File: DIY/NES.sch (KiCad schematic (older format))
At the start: 6 parts, among them J1 Conn_01x07, J2 Conn_01x07, J3 DB15_Female, J4 DB25_Male, U1 74AHCT125N, U2 74AHCT125N

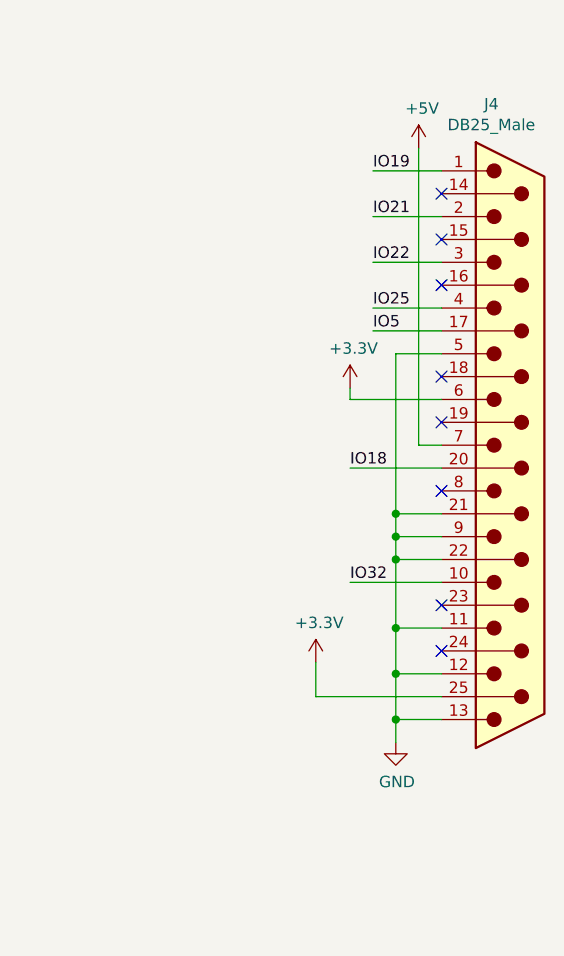
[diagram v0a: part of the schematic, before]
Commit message: [DIY] Update DIY & cable adapter schematic base on new DB25 mapping
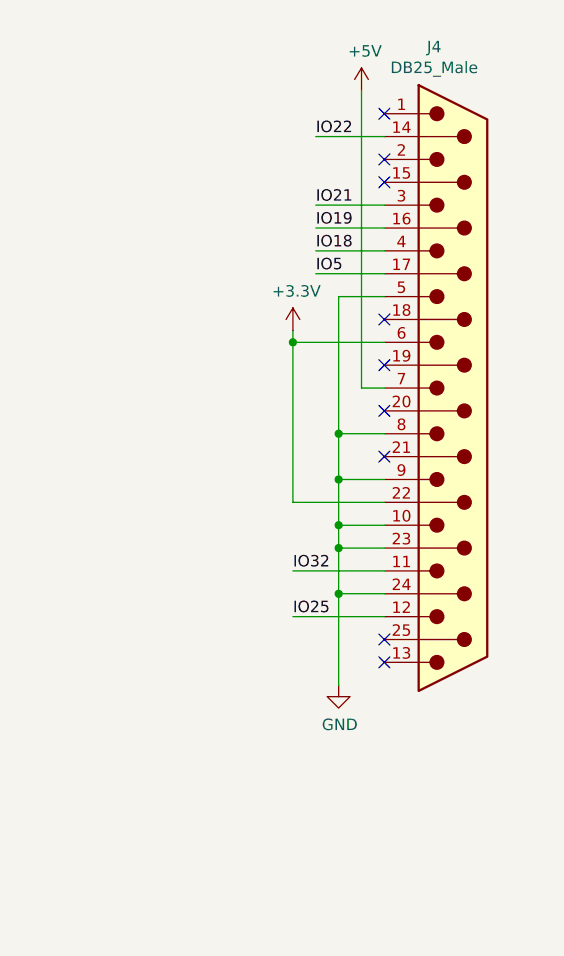
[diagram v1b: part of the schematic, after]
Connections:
- net +3V3: now also J4.22 (P22); no longer J4.25 (P25)
- net GND: now also J4.10, J4.23 (P23), J4.24 (P24), J4.8; no longer J4.11, J4.12, J4.13, J4.21 (P21), J4.22 (P22)
- net IO18: now also J4.4; no longer J4.20 (P20)
- net IO19: now also J4.16 (P16); no longer J4.1
- net IO21: now also J4.3; no longer J4.2
- net IO22: now also J4.14 (P14); no longer J4.3
- net IO25: now also J4.12; no longer J4.4
- net IO32: now also J4.11; no longer J4.10
- no-connect marks 27 -> 28
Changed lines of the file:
@@
 $Descr USLetter 11000 8500
 encoding utf-8
-Sheet 3 4
+Sheet 3 7
 Title "BlueRetro - Famicom/NES adapter cable"
-Date "2020-07-25"
-Rev "v1.0"
+Date "2020-08-22"
+Rev "v1.1"
 Comp ""
 Comment1 ""
@@
 $EndComp
 $Comp
-L Connector:DB25_Male J?
-U 1 1 5F23BC98
-P 10000 2850
-AR Path="/5F127084/5F23BC98" Ref="J?"  Part="1"
-AR Path="/5F1E85DD/5F23BC98" Ref="J4"  Part="1"
-F 0 "J4" H 9918 1358 50  0000 C CNN
-F 1 "DB25_Male" H 9918 1449 50  0000 C CNN
-F 2 "" H 10000 2850 50  0001 C CNN
-F 3 " ~" H 10000 2850 50  0001 C CNN
-	1    10000 2850
-	1    0    0    1
-$EndComp
-$Comp
 L 74xx:74LS125 U?
 U 1 1 5F23BCA4
@@
 F 3 "http://www.ti.com/general/docs/suppproductinfo.tsp?distId=10&gotoUrl=http%3A%2F%2Fwww.ti.com%2Flit%2Fgpn%2Fsn74ahct125" H 4150 5500 50  0001 C CNN
 	5    4150 5500
-	1    0    0    -1
-$EndComp
-Wire Wire Line
-	9400 1650 9700 1650
-Wire Wire Line
-	9400 1850 9700 1850
-Wire Wire Line
-	9400 2050 9700 2050
-Wire Wire Line
-	9400 2250 9700 2250
-$Comp
-L power:+5V #PWR?
-U 1 1 5F23BD02
-P 9600 1550
-AR Path="/5F127084/5F23BD02" Ref="#PWR?"  Part="1"
-AR Path="/5F1E85DD/5F23BD02" Ref="#PWR?"  Part="1"
-F 0 "#PWR?" H 9600 1400 50  0001 C CNN
-F 1 "+5V" H 9615 1723 50  0000 C CNN
-F 2 "" H 9600 1550 50  0001 C CNN
-F 3 "" H 9600 1550 50  0001 C CNN
-	1    9600 1550
-	1    0    0    -1
-$EndComp
-$Comp
-L power:GND #PWR?
-U 1 1 5F23BD08
-P 9500 4150
-AR Path="/5F127084/5F23BD08" Ref="#PWR?"  Part="1"
-AR Path="/5F1E85DD/5F23BD08" Ref="#PWR?"  Part="1"
-F 0 "#PWR?" H 9500 3900 50  0001 C CNN
-F 1 "GND" H 9505 3977 50  0000 C CNN
-F 2 "" H 9500 4150 50  0001 C CNN
-F 3 "" H 9500 4150 50  0001 C CNN
-	1    9500 4150
-	1    0    0    -1
-$EndComp
-Wire Wire Line
-	9700 2450 9500 2450
-Wire Wire Line
-	9500 2450 9500 3150
-Wire Wire Line
-	9700 3250 9500 3250
-Connection ~ 9500 3250
-Wire Wire Line
-	9600 1550 9600 2850
-Wire Wire Line
-	9600 2850 9700 2850
-$Comp
-L power:+3.3V #PWR?
-U 1 1 5F23BD18
-P 9300 2600
-AR Path="/5F127084/5F23BD18" Ref="#PWR?"  Part="1"
-AR Path="/5F1E85DD/5F23BD18" Ref="#PWR?"  Part="1"
-F 0 "#PWR?" H 9300 2450 50  0001 C CNN
-F 1 "+3.3V" H 9315 2773 50  0000 C CNN
-F 2 "" H 9300 2600 50  0001 C CNN
-F 3 "" H 9300 2600 50  0001 C CNN
-	1    9300 2600
 	1    0    0    -1
 $EndComp
@@
 	1    0    0    -1
 $EndComp
-Text Label 9400 1650 0    50   ~ 0
-IO19
-Text Label 9400 1850 0    50   ~ 0
-IO21
-Text Label 9400 2050 0    50   ~ 0
-IO22
-Text Label 9400 2250 0    50   ~ 0
-IO25
-Wire Wire Line
-	9700 2350 9400 2350
-Wire Wire Line
-	9300 2650 9300 2600
-Wire Wire Line
-	9300 2650 9700 2650
-Wire Wire Line
-	9300 2950 9700 2950
-NoConn ~ 9700 1950
-NoConn ~ 9700 2550
-NoConn ~ 9700 2750
-NoConn ~ 9700 3050
-Text Label 9400 2350 0    50   ~ 0
-IO5
-Text Label 9300 2950 0    50   ~ 0
-IO18
 $Comp
 L Connector:DB15_Female J3
@@
 NoConn ~ 1500 2250
 NoConn ~ 1500 2350
-Wire Wire Line
-	9500 3250 9500 3350
-$Comp
-L power:+3.3V #PWR?
-U 1 1 5F23310B
-P 9150 3800
-AR Path="/5F127084/5F23310B" Ref="#PWR?"  Part="1"
-AR Path="/5F1E85DD/5F23310B" Ref="#PWR?"  Part="1"
-F 0 "#PWR?" H 9150 3650 50  0001 C CNN
-F 1 "+3.3V" H 9165 3973 50  0000 C CNN
-F 2 "" H 9150 3800 50  0001 C CNN
-F 3 "" H 9150 3800 50  0001 C CNN
-	1    9150 3800
-	1    0    0    -1
-$EndComp
-Wire Wire Line
-	9700 3950 9150 3950
-Wire Wire Line
-	9150 3950 9150 3800
-Wire Wire Line
-	9700 4050 9500 4050
-Connection ~ 9500 4050
-Wire Wire Line
-	9500 4050 9500 4150
-Wire Wire Line
-	9700 3850 9500 3850
-Connection ~ 9500 3850
-Wire Wire Line
-	9500 3850 9500 4050
-Wire Wire Line
-	9700 3650 9500 3650
-Connection ~ 9500 3650
-Wire Wire Line
-	9500 3650 9500 3850
-Wire Wire Line
-	9700 3450 9300 3450
-Text Label 9300 3450 0    50   ~ 0
-IO32
-NoConn ~ 9700 1750
-NoConn ~ 9700 2150
-Wire Wire Line
-	9700 3150 9500 3150
-Connection ~ 9500 3150
-Wire Wire Line
-	9500 3150 9500 3250
-Wire Wire Line
-	9700 3350 9500 3350
-Connection ~ 9500 3350
-Wire Wire Line
-	9500 3350 9500 3650
-NoConn ~ 9700 3550
-NoConn ~ 9700 3750
 Text Label 3550 1350 0    50   ~ 0
 IO19
@@
 $EndComp
 NoConn ~ 7200 4100
+$Comp
+L Connector:DB25_Male J?
+U 1 1 5F70CF6E
+P 9750 2600
+AR Path="/5F127084/5F70CF6E" Ref="J?"  Part="1"
+AR Path="/5F1E85DD/5F70CF6E" Ref="J4"  Part="1"
+AR Path="/5F2C5C0D/5F70CF6E" Ref="J?"  Part="1"
+F 0 "J4" H 9668 1108 50  0000 C CNN
+F 1 "DB25_Male" H 9668 1199 50  0000 C CNN
+F 2 "" H 9750 2600 50  0001 C CNN
+F 3 " ~" H 9750 2600 50  0001 C CNN
+	1    9750 2600
+	1    0    0    1
+$EndComp
+Wire Wire Line
+	9150 1800 9450 1800
+Wire Wire Line
+	9150 2000 9450 2000
+$Comp
+L power:+5V #PWR?
+U 1 1 5F70CF77
+P 9350 1300
+AR Path="/5F127084/5F70CF77" Ref="#PWR?"  Part="1"
+AR Path="/5F1E85DD/5F70CF77" Ref="#PWR?"  Part="1"
+AR Path="/5F2C5C0D/5F70CF77" Ref="#PWR?"  Part="1"
+F 0 "#PWR?" H 9350 1150 50  0001 C CNN
+F 1 "+5V" H 9365 1473 50  0000 C CNN
+F 2 "" H 9350 1300 50  0001 C CNN
+F 3 "" H 9350 1300 50  0001 C CNN
+	1    9350 1300
+	1    0    0    -1
+$EndComp
+$Comp
+L power:GND #PWR?
+U 1 1 5F70CF7D
+P 9250 3900
+AR Path="/5F127084/5F70CF7D" Ref="#PWR?"  Part="1"
+AR Path="/5F1E85DD/5F70CF7D" Ref="#PWR?"  Part="1"
+AR Path="/5F2C5C0D/5F70CF7D" Ref="#PWR?"  Part="1"
+F 0 "#PWR?" H 9250 3650 50  0001 C CNN
+F 1 "GND" H 9255 3727 50  0000 C CNN
+F 2 "" H 9250 3900 50  0001 C CNN
+F 3 "" H 9250 3900 50  0001 C CNN
+	1    9250 3900
+	1    0    0    -1
+$EndComp
+Wire Wire Line
+	9450 2200 9250 2200
+Wire Wire Line
+	9450 3000 9250 3000
+Wire Wire Line
+	9350 1300 9350 2600
+Wire Wire Line
+	9350 2600 9450 2600
+$Comp
+L power:+3.3V #PWR?
+U 1 1 5F70CF87
+P 9050 2350
+AR Path="/5F127084/5F70CF87" Ref="#PWR?"  Part="1"
+AR Path="/5F1E85DD/5F70CF87" Ref="#PWR?"  Part="1"
+AR Path="/5F2C5C0D/5F70CF87" Ref="#PWR?"  Part="1"
+F 0 "#PWR?" H 9050 2200 50  0001 C CNN
+F 1 "+3.3V" H 9065 2523 50  0000 C CNN
+F 2 "" H 9050 2350 50  0001 C CNN
+F 3 "" H 9050 2350 50  0001 C CNN
+	1    9050 2350
+	1    0    0    -1
+$EndComp
+Text Label 9150 1900 0    50   ~ 0
+IO19
+Text Label 9150 1800 0    50   ~ 0
+IO21
+Text Label 9150 1500 0    50   ~ 0
+IO22
+Text Label 9050 3600 0    50   ~ 0
+IO25
+Wire Wire Line
+	9450 2100 9150 2100
+Wire Wire Line
+	9050 2400 9050 2350
+Wire Wire Line
+	9050 2400 9450 2400
+Text Label 9150 2100 0    50   ~ 0
+IO5
+Text Label 9150 2000 0    50   ~ 0
+IO18
+Text Label 9050 3400 0    50   ~ 0
+IO32
+Wire Wire Line
+	9250 2200 9250 2800
+Wire Wire Line
+	9250 3900 9250 3500
+Connection ~ 9250 3000
+Wire Wire Line
+	9450 2800 9250 2800
+Connection ~ 9250 2800
+Wire Wire Line
+	9250 2800 9250 3000
+Wire Wire Line
+	9450 1900 9150 1900
+Wire Wire Line
+	9450 1500 9150 1500
+Wire Wire Line
+	9450 3600 9050 3600
+Wire Wire Line
+	9450 3400 9050 3400
+NoConn ~ 9450 3800
+NoConn ~ 9450 1600
+NoConn ~ 9450 1700
+NoConn ~ 9450 2300
+NoConn ~ 9450 2500
+NoConn ~ 9450 2700
+NoConn ~ 9450 2900
+Wire Wire Line
+	9450 3200 9250 3200
+Connection ~ 9250 3200
+Wire Wire Line
+	9450 3300 9250 3300
+Connection ~ 9250 3300
+Wire Wire Line
+	9250 3300 9250 3200
+Wire Wire Line
+	9450 3500 9250 3500
+Connection ~ 9250 3500
+Wire Wire Line
+	9250 3500 9250 3300
+NoConn ~ 9450 1400
+NoConn ~ 9450 3700
+Wire Wire Line
+	9250 3000 9250 3200
+Wire Wire Line
+	9450 3100 9050 3100
+Wire Wire Line
+	9050 3100 9050 2400
+Connection ~ 9050 2400
 $EndSCHEMATC

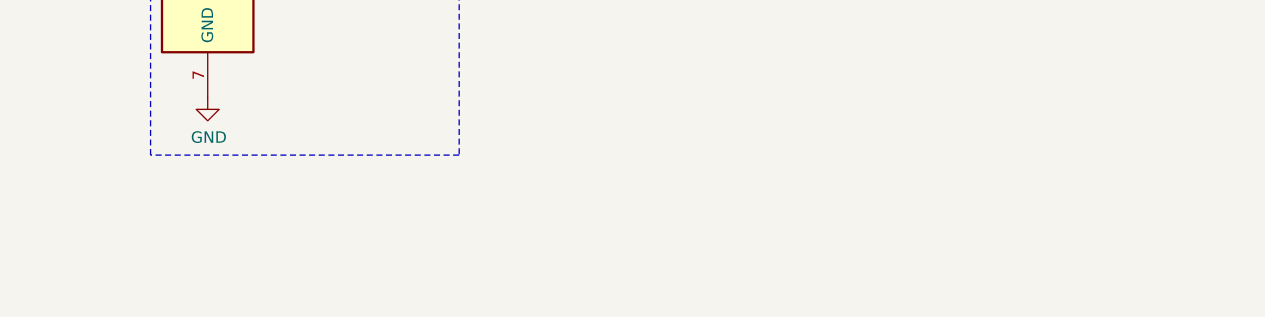
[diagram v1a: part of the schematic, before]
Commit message: [DIY] Add note to cable schematics to underline how important I39 is.
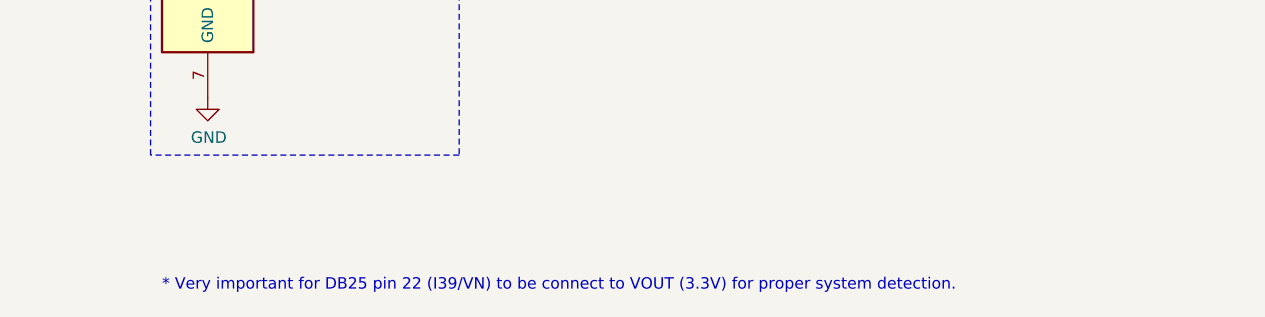
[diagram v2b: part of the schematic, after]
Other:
- note added: "* Very important for DB25 pin 22 (I39/VN) to be connect to VOUT (3.3V) for proper system detection."
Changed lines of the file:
@@
 	9050 3100 9050 2400
 Connection ~ 9050 2400
+Text Notes 6350 6900 0    50   ~ 0
+* Very important for DB25 pin 22 (I39/VN) to be connect to VOUT (3.3V) for proper system detection.
 $EndSCHEMATC

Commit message: Use new port symbol in cable schematic
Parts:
- J1, J2: symbol Connector_Generic:Conn_01x07 -> Connector_Gaming:NES
- J3: symbol Connector:DB15_Female -> Connector_Gaming:Atari5200_Famicom_NeoGeoAES_PCGamePort_DA15
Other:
- note added: "Connectors facing console"
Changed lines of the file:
@@
 Sheet 3 7
 Title "BlueRetro - Famicom/NES adapter cable"
-Date "2020-08-22"
-Rev "v1.1"
-Comp ""
+Date "2020-10-02"
+Rev "v1.2"
+Comp "©2020 Jacques Gagnon, licensed under CC-BY-4.0"
 Comment1 ""
 Comment2 ""
@@
 IO18
 $Comp
-L Connector_Generic:Conn_01x07 J?
-U 1 1 5F23BDF9
-P 1300 2050
-AR Path="/5F127084/5F23BDF9" Ref="J?"  Part="1"
-AR Path="/5F1E85DD/5F23BDF9" Ref="J1"  Part="1"
-F 0 "J1" H 1300 2600 50  0000 C CNN
-F 1 "Conn_01x07" H 1300 2500 50  0000 C CNN
-F 2 "" H 1300 2050 50  0001 C CNN
-F 3 "~" H 1300 2050 50  0001 C CNN
-	1    1300 2050
-	-1   0    0    -1
-$EndComp
-$Comp
-L Connector_Generic:Conn_01x07 J?
+L Connector_Gaming:NES J?
 U 1 1 5F23BDFF
-P 1300 3900
+P 1900 2900
 AR Path="/5F127084/5F23BDFF" Ref="J?"  Part="1"
 AR Path="/5F1E85DD/5F23BDFF" Ref="J2"  Part="1"
-F 0 "J2" H 1300 4450 50  0000 C CNN
-F 1 "Conn_01x07" H 1300 4350 50  0000 C CNN
-F 2 "" H 1300 3900 50  0001 C CNN
-F 3 "~" H 1300 3900 50  0001 C CNN
-	1    1300 3900
-	-1   0    0    -1
+F 0 "J2" H 1950 3250 50  0000 C CNN
+F 1 "Conn_01x07" H 1900 3350 50  0001 C CNN
+F 2 "" H 1900 2900 50  0001 C CNN
+F 3 "~" H 1900 2900 50  0001 C CNN
+	1    1900 2900
+	1    0    0    -1
 $EndComp
 $Comp
 L power:GND #PWR?
 U 1 1 5F23BE05
-P 1600 2450
+P 1600 2050
 AR Path="/5F127084/5F23BE05" Ref="#PWR?"  Part="1"
 AR Path="/5F1E85DD/5F23BE05" Ref="#PWR?"  Part="1"
-F 0 "#PWR?" H 1600 2200 50  0001 C CNN
-F 1 "GND" H 1605 2277 50  0000 C CNN
-F 2 "" H 1600 2450 50  0001 C CNN
-F 3 "" H 1600 2450 50  0001 C CNN
-	1    1600 2450
-	1    0    0    -1
+F 0 "#PWR?" H 1600 1800 50  0001 C CNN
+F 1 "GND" H 1605 1877 50  0000 C CNN
+F 2 "" H 1600 2050 50  0001 C CNN
+F 3 "" H 1600 2050 50  0001 C CNN
+	1    1600 2050
+	-1   0    0    -1
 $EndComp
 $Comp
 L power:GND #PWR?
 U 1 1 5F23BE0B
-P 1600 4300
+P 1600 3050
 AR Path="/5F127084/5F23BE0B" Ref="#PWR?"  Part="1"
 AR Path="/5F1E85DD/5F23BE0B" Ref="#PWR?"  Part="1"
-F 0 "#PWR?" H 1600 4050 50  0001 C CNN
-F 1 "GND" H 1605 4127 50  0000 C CNN
-F 2 "" H 1600 4300 50  0001 C CNN
-F 3 "" H 1600 4300 50  0001 C CNN
-	1    1600 4300
-	1    0    0    -1
+F 0 "#PWR?" H 1600 2800 50  0001 C CNN
+F 1 "GND" H 1605 2877 50  0000 C CNN
+F 2 "" H 1600 3050 50  0001 C CNN
+F 3 "" H 1600 3050 50  0001 C CNN
+	1    1600 3050
+	-1   0    0    -1
 $EndComp
 $Comp
 L power:+5V #PWR?
 U 1 1 5F23BE11
-P 1650 3450
+P 2300 2650
 AR Path="/5F127084/5F23BE11" Ref="#PWR?"  Part="1"
 AR Path="/5F1E85DD/5F23BE11" Ref="#PWR?"  Part="1"
-F 0 "#PWR?" H 1650 3300 50  0001 C CNN
-F 1 "+5V" H 1665 3623 50  0000 C CNN
-F 2 "" H 1650 3450 50  0001 C CNN
-F 3 "" H 1650 3450 50  0001 C CNN
-	1    1650 3450
+F 0 "#PWR?" H 2300 2500 50  0001 C CNN
+F 1 "+5V" H 2315 2823 50  0000 C CNN
+F 2 "" H 2300 2650 50  0001 C CNN
+F 3 "" H 2300 2650 50  0001 C CNN
+	1    2300 2650
 	1    0    0    -1
 $EndComp
@@
 L power:+5V #PWR?
 U 1 1 5F23BE17
-P 1650 1600
+P 2300 1700
 AR Path="/5F127084/5F23BE17" Ref="#PWR?"  Part="1"
 AR Path="/5F1E85DD/5F23BE17" Ref="#PWR?"  Part="1"
-F 0 "#PWR?" H 1650 1450 50  0001 C CNN
-F 1 "+5V" H 1665 1773 50  0000 C CNN
-F 2 "" H 1650 1600 50  0001 C CNN
-F 3 "" H 1650 1600 50  0001 C CNN
-	1    1650 1600
-	1    0    0    -1
-$EndComp
-$Comp
-L Connector:DB15_Female J3
+F 0 "#PWR?" H 2300 1550 50  0001 C CNN
+F 1 "+5V" H 2315 1873 50  0000 C CNN
+F 2 "" H 2300 1700 50  0001 C CNN
+F 3 "" H 2300 1700 50  0001 C CNN
+	1    2300 1700
+	1    0    0    -1
+$EndComp
+$Comp
+L Connector_Gaming:Atari5200_Famicom_NeoGeoAES_PCGamePort_DA15 J3
 U 1 1 5F2B655C
-P 1200 6100
-F 0 "J3" H 1106 7092 50  0000 C CNN
-F 1 "DB15_Female" H 1106 7001 50  0000 C CNN
-F 2 "" H 1200 6100 50  0001 C CNN
-F 3 " ~" H 1200 6100 50  0001 C CNN
-	1    1200 6100
-	-1   0    0    -1
-$EndComp
-Wire Wire Line
-	1500 6300 1800 6300
-Wire Wire Line
-	1500 6600 1800 6600
-Text Notes 750  5050 0    50   ~ 0
+P 1900 4250
+F 0 "J3" H 1900 3400 50  0000 C CNN
+F 1 "DB15_Female" H 1806 5151 50  0001 C CNN
+F 2 "" H 1900 4250 50  0001 C CNN
+F 3 " ~" H 1900 4250 50  0001 C CNN
+	1    1900 4250
+	-1   0    0    1
+$EndComp
+Wire Wire Line
+	2200 4450 2500 4450
+Wire Wire Line
+	2200 4750 2500 4750
+Text Notes 1450 3200 0    50   ~ 0
 *Optional (only for Famicom 4P)
-NoConn ~ 1500 5400
-NoConn ~ 1500 5500
-NoConn ~ 1500 5600
-NoConn ~ 1500 5700
-NoConn ~ 1500 5800
-NoConn ~ 1500 5900
-NoConn ~ 1500 6000
-NoConn ~ 1500 6100
-NoConn ~ 1500 6200
-NoConn ~ 1500 6400
-NoConn ~ 1500 6500
-NoConn ~ 1500 6700
-NoConn ~ 1500 6800
-Text Label 1800 6300 2    50   ~ 0
+NoConn ~ 2200 3550
+NoConn ~ 2200 3650
+NoConn ~ 2200 3750
+NoConn ~ 2200 3850
+NoConn ~ 2200 3950
+NoConn ~ 2200 4050
+NoConn ~ 2200 4150
+NoConn ~ 2200 4250
+NoConn ~ 2200 4350
+NoConn ~ 2200 4550
+NoConn ~ 2200 4650
+NoConn ~ 2200 4850
+NoConn ~ 2200 4950
+Text Label 2500 4450 2    50   ~ 0
 P1-D1
-Text Label 1800 6600 2    50   ~ 0
+Text Label 2500 4750 2    50   ~ 0
 P2-D1
 Wire Wire Line
-	1500 3600 1600 3600
-Wire Wire Line
-	1500 4000 1650 4000
-Wire Wire Line
-	1650 4000 1650 3450
-Text Label 2000 3700 2    50   ~ 0
+	1700 2700 1600 2700
+Text Label 1200 2800 0    50   ~ 0
 P2-CUP
 Wire Wire Line
-	1500 3700 2000 3700
-Wire Wire Line
-	1500 3900 2000 3900
-NoConn ~ 1500 4100
-NoConn ~ 1500 4200
-NoConn ~ 1500 3800
-Text Label 2000 3900 2    50   ~ 0
+	1700 2800 1200 2800
+Wire Wire Line
+	1700 3000 1200 3000
+NoConn ~ 2200 2900
+NoConn ~ 2200 3000
+NoConn ~ 1700 2900
+Text Label 1200 3000 0    50   ~ 0
 P2-D0
 Wire Wire Line
-	1600 3600 1600 4300
-Wire Wire Line
-	1500 2150 1650 2150
-Wire Wire Line
-	1650 1600 1650 2150
-Wire Wire Line
-	1500 1750 1600 1750
-Wire Wire Line
-	1600 1750 1600 2450
-Wire Wire Line
-	1500 1850 2000 1850
-Wire Wire Line
-	1500 1950 2000 1950
-Wire Wire Line
-	1500 2050 2000 2050
-Text Label 2000 1850 2    50   ~ 0
+	1600 2700 1600 3050
+Wire Wire Line
+	1700 1700 1600 1700
+Wire Wire Line
+	1700 1800 1200 1800
+Text Label 1200 1800 0    50   ~ 0
 P1-CUP
-Text Label 2000 1950 2    50   ~ 0
+Text Label 1200 1900 0    50   ~ 0
 OUT0
-Text Label 2000 2050 2    50   ~ 0
+Text Label 1200 2000 0    50   ~ 0
 P1-D0
-NoConn ~ 1500 2250
-NoConn ~ 1500 2350
+NoConn ~ 2200 1900
+NoConn ~ 2200 2000
 Text Label 3550 1350 0    50   ~ 0
 IO19
@@
 Text Notes 6350 6900 0    50   ~ 0
 * Very important for DB25 pin 22 (I39/VN) to be connect to VOUT (3.3V) for proper system detection.
+Wire Wire Line
+	1700 2000 1200 2000
+Wire Wire Line
+	1700 1900 1200 1900
+Wire Wire Line
+	1600 1700 1600 2050
+$Comp
+L Connector_Gaming:NES J?
+U 1 1 5F23BDF9
+P 1900 1900
+AR Path="/5F127084/5F23BDF9" Ref="J?"  Part="1"
+AR Path="/5F1E85DD/5F23BDF9" Ref="J1"  Part="1"
+F 0 "J1" H 1950 2250 50  0000 C CNN
+F 1 "Conn_01x07" H 1900 2350 50  0001 C CNN
+F 2 "" H 1900 1900 50  0001 C CNN
+F 3 "~" H 1900 1900 50  0001 C CNN
+	1    1900 1900
+	1    0    0    -1
+$EndComp
+Wire Wire Line
+	2200 1800 2300 1800
+Wire Wire Line
+	2300 1800 2300 1700
+Text Notes 1750 2350 0    50   ~ 0
+Connectors facing console
+Wire Wire Line
+	2200 2800 2300 2800
+Wire Wire Line
+	2300 2800 2300 2650
 $EndSCHEMATC
